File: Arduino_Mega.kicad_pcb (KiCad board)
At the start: 2 copper layers, 101.6 x 58.2 mm, 33 parts, among them P1 Digital, P14 SERVO_OUT_0, P15 SERVO_OUT_1, P16 SERVO_OUT_2, P17 SERVO_OUT_3, P18 SERVO_OUT_4, P19 SERVO_OUT_5, P2 Power, P20 5V+, P21 5V-, P23 SENOSRS_IN, P3 Analog, P4 Analog, P5 PWM, P6 PWM, P7 Communication, P8 5V_SERVO_JP, P9 PWR_OUT, SW1 RST

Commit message: pcb rev2
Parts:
- removed P1: Digital, Socket_Arduino_Mega:Socket_Strip_Arduino_2x18
- removed P20: 5V+, Pin_Headers:Pin_Header_Straight_1x01
- removed P21: 5V-, Pin_Headers:Pin_Header_Straight_1x01
- added P10: CONN_2, Terminal_Blocks:TerminalBlock_Pheonix_MKDS1.5-2pol, F.Cu at (190.8, 74.9)
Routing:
- net +5V: track 138.8 -> 174.5 mm
- net /VoltageDivider/ADC8: track 35.4 -> 34.8 mm

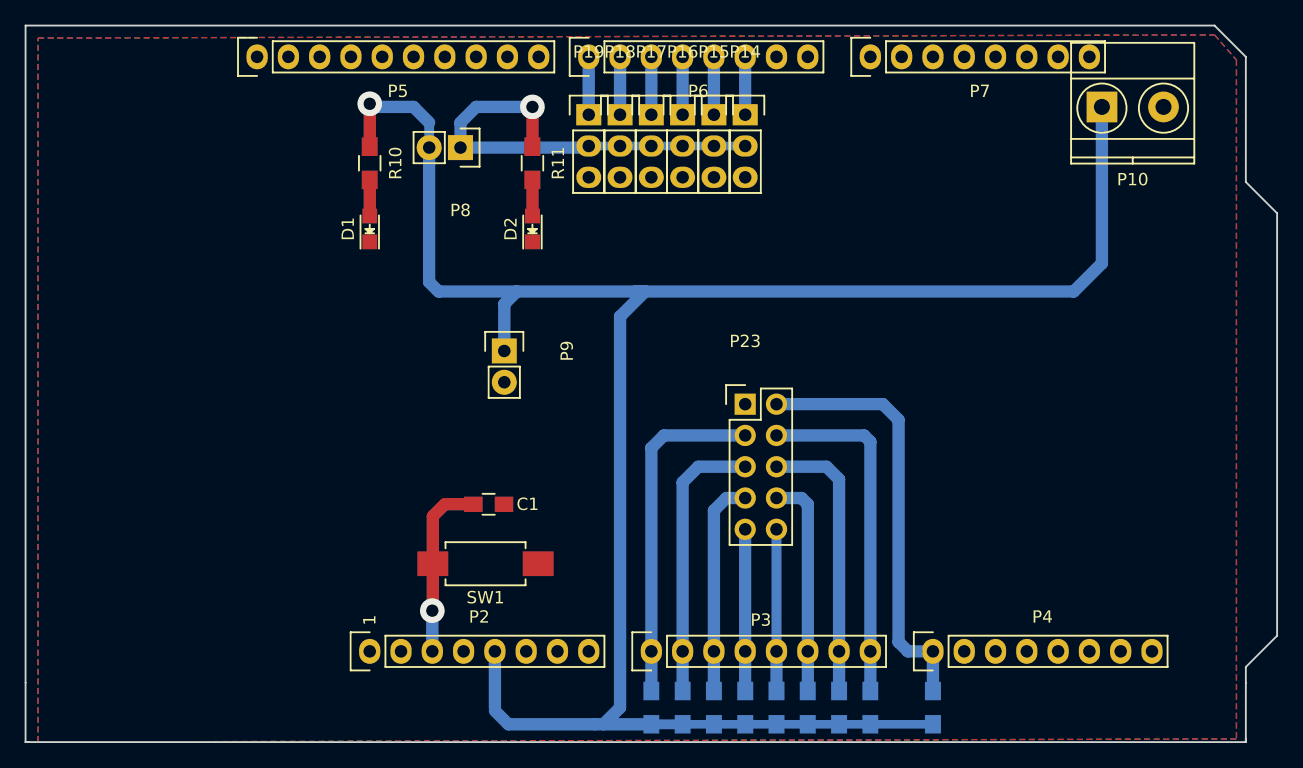
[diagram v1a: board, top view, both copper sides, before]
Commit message: Jumper removed, pdf generated
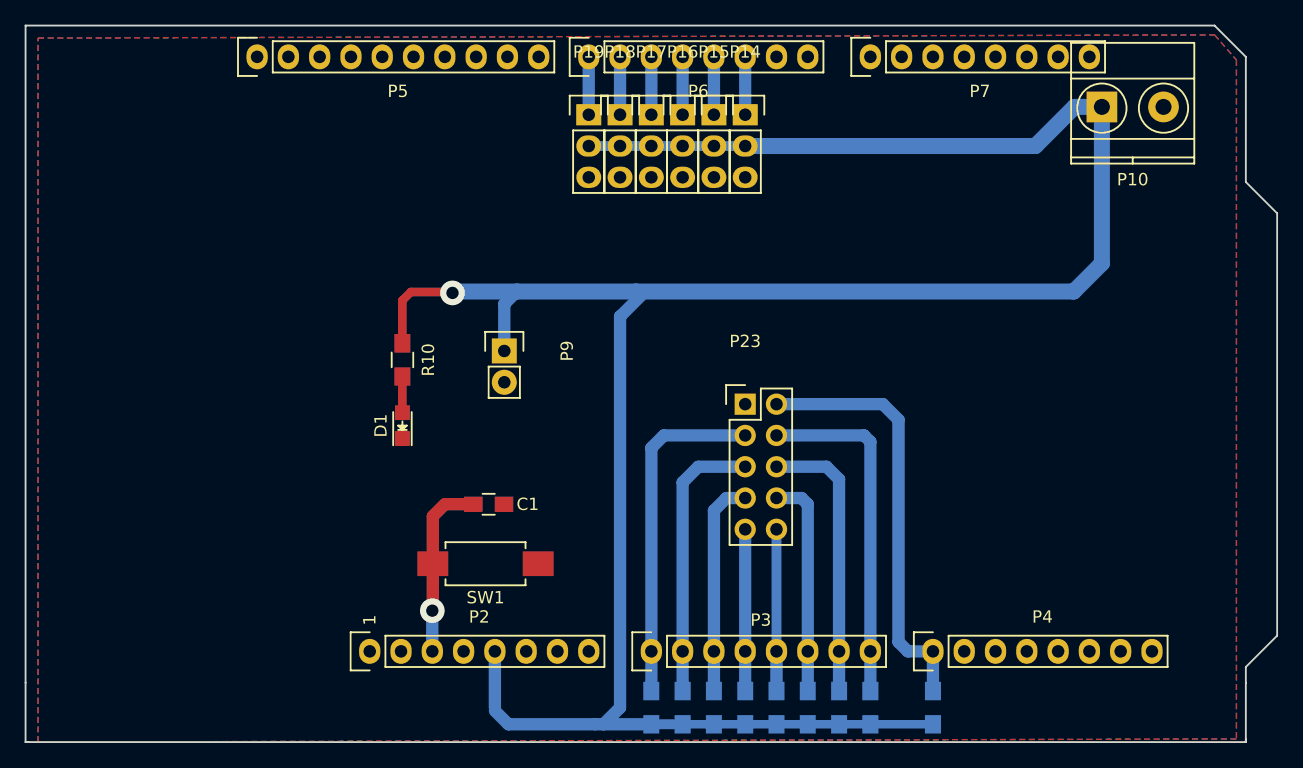
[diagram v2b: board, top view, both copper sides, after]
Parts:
- removed D2: SERVO_POWER_LED, LEDs:LED_0805
- removed P8: 5V_SERVO_JP, Socket_Strips:Socket_Strip_Straight_1x02
- removed R11: 150, Resistors_SMD:R_0805_HandSoldering
- moved R10 16.2 mm to (134.0, 95.5)
- moved D1 16.2 mm to (134.0, 100.8)
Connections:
- P14 pad 2: 5V_SERVO -> +5V
- P15 pad 2: 5V_SERVO -> +5V
- P16 pad 2: 5V_SERVO -> +5V
- P17 pad 2: 5V_SERVO -> +5V
- P18 pad 2: 5V_SERVO -> +5V
- P19 pad 2: 5V_SERVO -> +5V
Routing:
- net 5V_SERVO: track 34.9 -> 0.00 mm, vias 1 -> 0
- net +5V: track 174.5 -> 201.5 mm
- net Net-(D2-Pad2): track 2.93 -> 0.00 mm
